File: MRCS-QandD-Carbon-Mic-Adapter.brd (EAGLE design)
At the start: 106 x 100 mm, 4 parts

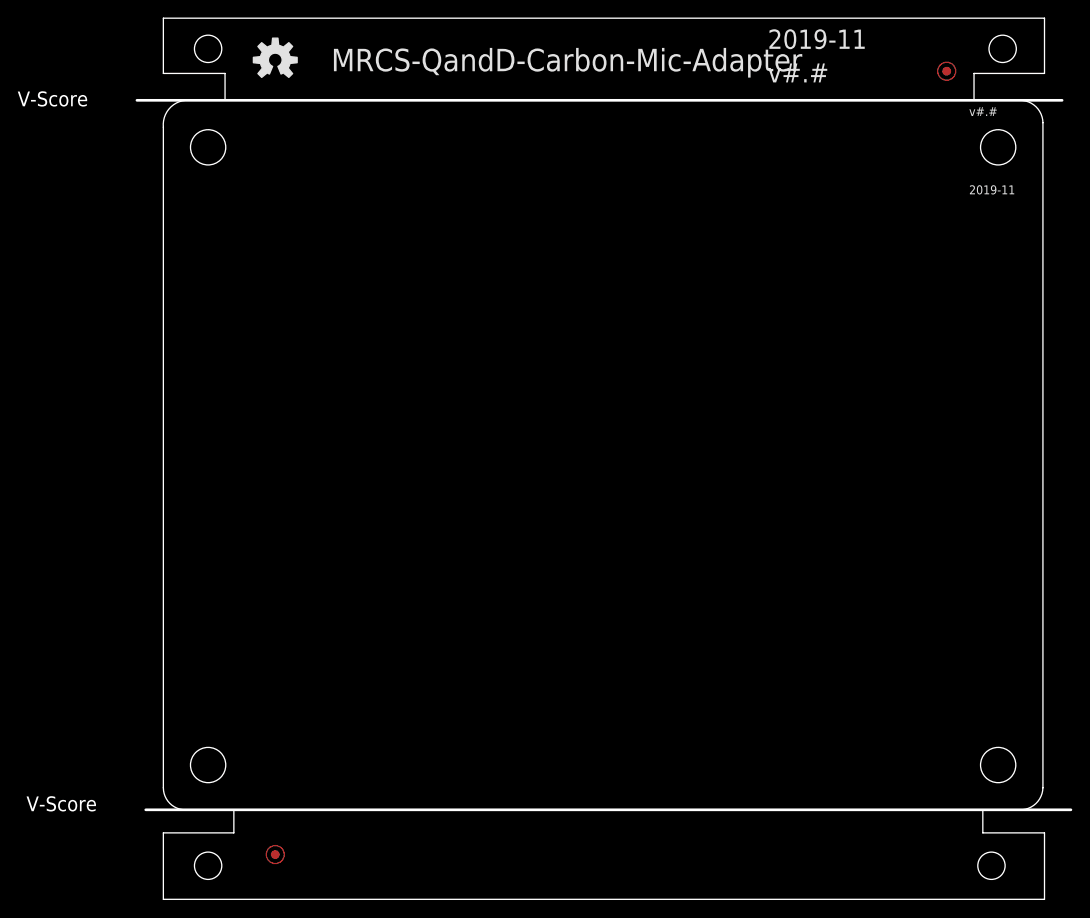
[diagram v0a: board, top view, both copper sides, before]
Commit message: Initial design sent to PCB Fab on 1/2/22
First pass board, easier to make the PCB than fool with a bread board.
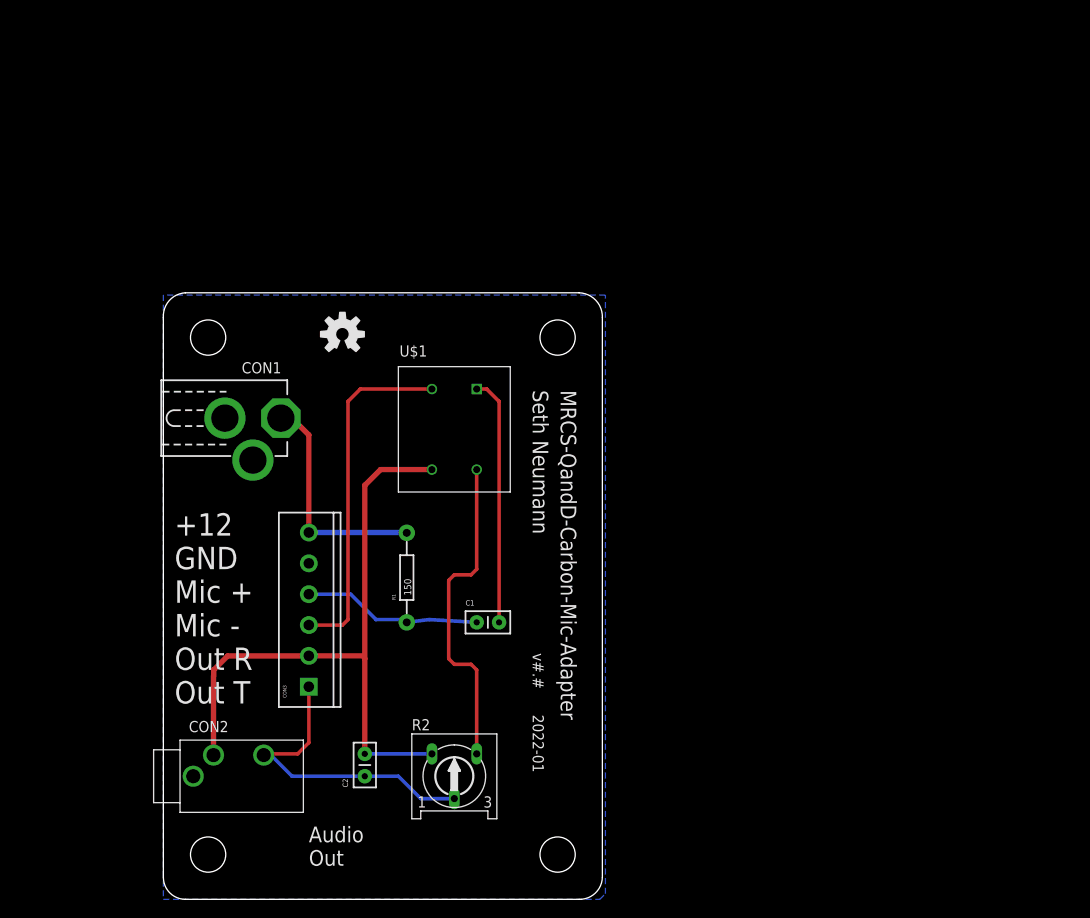
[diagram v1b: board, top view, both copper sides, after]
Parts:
- removed BOARD1: BOARD80X100, SPCoast:BOARD-DINRAIL-3.17INX10CM
- removed FID1, FID2: FIDUCIAL, SPCoast:FIDUCIAL_1MM
- added C1: 1.0 uF, SPCoast:C-PTH-0.100
- added C2: 0.1 uF, SPCoast:C-PTH-0.100
- added CON1: DC PWR, SPCoast:DCJ0202
- added CON2: Output, SPCoast:AUDIO-JACK-3.5MM_STEREO
- added CON3: (no value), SPCoast:SCREWTERMINAL-3.5MM-6
- added R1: 150, SPCoast:AXIAL-0.4-RES
- added R2: 1K, pot:RS3
- added U$1: EI14_600-600, MRCS:XFMR580X500
- added U$2: (no value), SPCoast:BOARD-DINRAIL-2.7IN-5CM
- added U$3: (no value), MRCSLogoTop:MRCSLOGOTOP
- added U$4: (no value), MRCS-prop65warningBtm:CA-PROP65WARNING
- moved OSHW1 32.0 mm to (20.3, 64.1)
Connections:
- new net +12V: CON1.1, CON3.6, R1.P$2
- new net GND: CON1.2, CON1.3, CON2.GND, CON3.5
- new net MIC+: C1.1, CON3.4, R1.P$1
- new net N$1: R2.E, U$1.STOP
- new net N$3: C1.2, U$1.PTOP
- new net N$7: C2.1, CON2.RING, CON3.1, R2.S
- new net OUTR: CON3.3, U$1.PBOTTOM
- new net OUTT: C2.2, CON2.TIP, CON3.2, R2.A, U$1.SBOTTOM
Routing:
- net OUTT: track 0.00 -> 74.1 mm
- net OUTR: track 0.00 -> 39.6 mm
- net N$1: track 0.00 -> 37.1 mm
- net N$7: track 0.00 -> 35.7 mm
- net N$3: track 0.00 -> 28.2 mm
- net +12V: track 0.00 -> 26.2 mm
- net MIC+: track 0.00 -> 20.4 mm
- added copper zone on layer 16, net GND
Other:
- board size 106 x 100 mm -> 49.8 x 68.8 mm
- board text added: "+12 GND Mic + Mic - Out R Out T"
- board text added: "2022-01"
- board text added: "Audio Out"
- board text added: "Seth Neumann"
- board text removed: "2019-11"
